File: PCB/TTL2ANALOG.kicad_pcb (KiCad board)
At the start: 2 copper layers, 31 parts, among them J1 EGA/CGA, J2 Brown Fix, J3 CSync Selection, J4 Sync Type, J5 TTL Input, J6 Analog Out, J7 Barrel_Jack, U1 GAL16V8, U2 74LS244, U3 74LS244, U4 L78L05_TO92

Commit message: Continue drawing PCB
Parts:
- added H1: MountingHole_Pad, MountingHole:MountingHole_3.2mm_M3_DIN965_Pad, F.Cu at (110.9, 102.7)
- added H2: MountingHole_Pad, MountingHole:MountingHole_3.2mm_M3_DIN965_Pad, F.Cu at (164.0, 102.7)
- added H3: MountingHole_Pad, MountingHole:MountingHole_3.2mm_M3_DIN965_Pad, F.Cu at (83.7, 66.2)
- added H4: MountingHole_Pad, MountingHole:MountingHole_3.2mm_M3_DIN965_Pad, F.Cu at (83.7, 73.3)
- C7: footprint Capacitor_THT:CP_Radial_D7.5mm_P2.50mm -> Capacitor_THT:CP_Radial_D6.3mm_P2.50mm
- moved C2 200.4 mm to (279.1, 79.1)
- moved R4 200.4 mm to (324.2, 106.3)
- moved R5 200.4 mm to (324.2, 108.8)
- moved R11 200.4 mm to (328.7, 77.7)
- moved R2 200.4 mm to (334.4, 106.3)
- moved R3 200.4 mm to (334.4, 108.8)
- moved R6 200.4 mm to (314.1, 108.8)
- moved R7 200.4 mm to (314.1, 106.3)
- moved R9 200.4 mm to (302.0, 97.4)
- moved C4 200.4 mm to (295.0, 110.1)
- moved C5 200.4 mm to (327.4, 94.9)
- moved C6 200.4 mm to (279.1, 82.5)
- moved D2 200.4 mm to (323.6, 80.3)
- moved J3 200.4 mm to (291.8, 117.1)
- moved J6 200.4 mm to (252.2, 74.8)
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
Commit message: Draw PCB
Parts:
- C1, C2, C3, C4, C5, C6, R10: moved to B.Cu
- R11, R8, R9: footprint Resistor_THT:R_Axial_DIN0204_L3.6mm_D1.6mm_P7.62mm_Horizontal -> Resistor_SMD:R_1206_3216Metric_Pad1.30x1.75mm_HandSolder; moved to B.Cu
- R6: footprint Resistor_THT:R_Axial_DIN0204_L3.6mm_D1.6mm_P7.62mm_Horizontal -> Resistor_SMD:R_1206_3216Metric_Pad1.30x1.75mm_HandSolder
- moved R2 213.4 mm to (125.7, 61.7), turned to 90 degrees
- moved R3 211.4 mm to (128.3, 61.7), turned to 90 degrees
- moved R11 207.9 mm to (120.8, 80.5), turned to 90 degrees
- moved D2 202.8 mm to (120.8, 80.5), turned to 270 degrees
- moved R4 197.3 mm to (132.1, 61.7), turned to 90 degrees
- moved R5 195.4 mm to (134.6, 61.7), turned to 90 degrees
- moved R9 187.7 mm to (116.0, 72.4), turned to 90 degrees
- moved R7 181.2 mm to (138.4, 61.7), turned to 90 degrees
- moved R6 179.4 mm to (141.0, 61.7), turned to 90 degrees
- moved R8 172.0 mm to (123.6, 72.4), turned to 90 degrees
- moved C5 171.2 mm to (158.0, 70.2), turned to 270 degrees
- moved R10 158.0 mm to (155.7, 56.0)
- moved C4 154.7 mm to (145.5, 70.2), turned to 270 degrees
- moved C6 147.3 mm to (132.3, 70.2), turned to 270 degrees
- moved J3 145.9 mm to (157.0, 61.3), turned to 270 degrees
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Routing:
- net GND: track 0.00 -> 274.2 mm
- net /IN_HS_BUF: track 0.00 -> 88.7 mm, vias 0 -> 1
- net VCC: track 0.00 -> 81.7 mm
- net /OUT_G_I: track 0.00 -> 63.1 mm
- net /IN_B: track 0.00 -> 45.8 mm
- net /OUT_CS: track 0.00 -> 45.5 mm
- net /~DEC_CS: track 0.00 -> 44.5 mm
- net /MODE: track 0.00 -> 43.1 mm
- net /BRWN_FIX: track 0.00 -> 42.2 mm
- net /IN_VS_BUF: track 0.00 -> 39.4 mm, vias 0 -> 1
- net /IN_VS: track 0.00 -> 38.4 mm
- net /IN_G_I: track 0.00 -> 36.5 mm
- net /DEC_G_I: track 0.00 -> 34.3 mm
- net /OUT_B: track 0.00 -> 33.8 mm, vias 0 -> 1
- net /~OUT_CS: track 0.00 -> 33.3 mm
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- added copper zone on B.Cu, net GND
- added copper zone on F.Cu, net GND
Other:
- board outline added: 60.5 x 56.1 mm
- board text removed: "B"
- board text removed: "Brown Fix Disable"
- board text removed: "EGA"
- board text removed: "G"
- board text removed: "GND"
- board text removed: "S"
- board text removed: "SYNC"

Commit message: Complete main circuit
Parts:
- J1, J2, J4: footprint Connector_PinSocket_2.54mm:PinSocket_1x03_P2.54mm_Vertical -> Connector_PinHeader_2.54mm:PinHeader_1x03_P2.54mm_Vertical
- J3: value CSync Selection -> CSync Inv.; footprint Connector_PinSocket_2.54mm:PinSocket_1x03_P2.54mm_Vertical -> Connector_PinHeader_2.54mm:PinHeader_1x03_P2.54mm_Vertical
- U4: value L78L05_TO92 -> L78L05

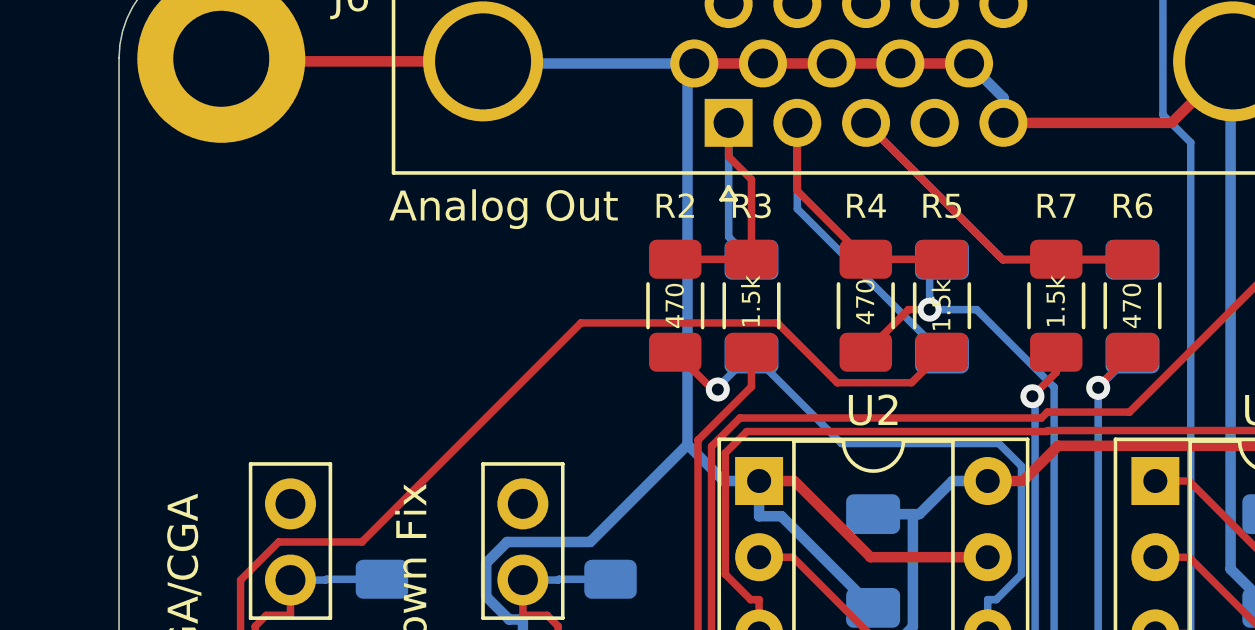
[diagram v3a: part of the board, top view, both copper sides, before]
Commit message: Add silkscreen
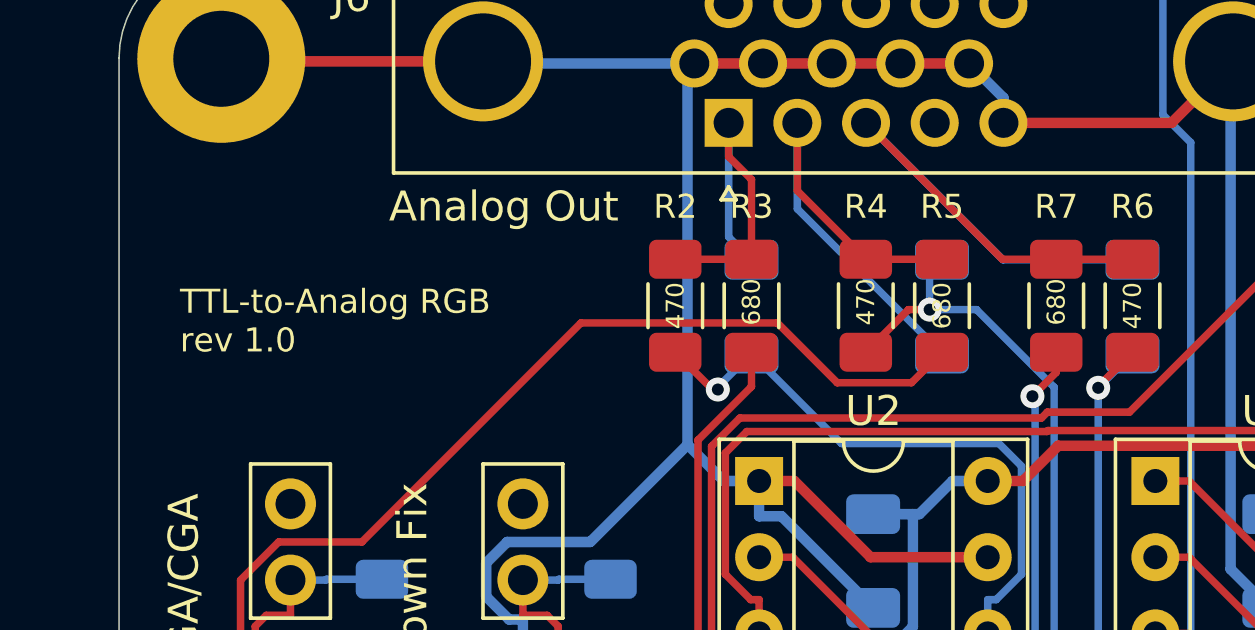
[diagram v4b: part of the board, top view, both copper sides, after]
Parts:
- R3, R5, R7: value 1.5k -> 680
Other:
- board text added: "TTL-to-Analog RGB rev 1.0"
